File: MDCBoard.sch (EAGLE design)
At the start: 202 parts, among them J1 JUMPER-SOLDER, J10 USB-C-RECEPTACLE-KOREANHRO, J2 JUMPER-SOLDER, J3 JUMPER-SOLDER, J4 JUMPER-SOLDER, J5 BATTERY-HEADER-MOLEX-781710002, J6 JUMPER-SOLDER, J7 JUMPER-SOLDER, J8 JUMPER-SOLDER, J9 MICROSD-SOCKET, Q1 PMOS-NEXPERIA-SOT1220, Q2 PMOS-NEXPERIA-SOT1220, Q3 PMOS-NEXPERIA-SOT1220, Q4 DIODESINC-DMG2305UX, Q5 DIODESINC-DMG2305UX, Q6 DIODESINC-DMG2305UX, Q7 DIODESINC-DMG2305UX, Q8 DIODESINC-DMG2305UX, SW1 TACTILE-SWITCH, U1 TI-TPS2116, U10 TI-TPS22919DCK, U11 TI-TPS22919DCK, U12 TI-TPS22919DCK, U13 TI-TPS22919DCK, U14 TI-MSP430FR2433IRGE, U15 TI-TXB0102, U16 PANASONIC-EKMB110711X, U17 LATTICE-ICE40HX4K-BG121, U18 WINBOND-W25Q40EW, U19 NEXPERIA-74LVC1G98-OR-INV-INP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, U2 DIODESINC-AP7350, U20 NEXPERIA-74LVC1G98-BUFFER, U21 ON-AR0330CS1C12SPKA0, U22 ALLIANCE-AS4C8M16MSA-6BIN, U23 NEXPERIA-74LVC1G98-INVERTER, U24 STM-STM32F730, U25 DIODESINC-DT1446-04V-7, U3 NEXPERIA-74LVC1G98-NOR, U4 MICROCHIP-MCP7383X, U5 NEXPERIA-74LVC1G98-INVERTER, U6 EATON-STN101, U7 TI-TPS62A01, U8 TI-TPS62A01, U9 TI-TPS62A01, X1 EPSON-FC-135, X2 SITIME-SIT8021, X3 SITIME-SIT8021

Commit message: Add comment
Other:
- note added: "Pullup to VDD_USB (TPS2116's VIN1, not its VOUT as shown in the datasheet) to avoid a leakage current that would exist when battery powered. If we did pullup to VDD_A (TPS2116's VOUT), ST would be driven to GND when battery powered, and we'd have a huge leakage current between VDD_A and GND (4.2V/10k = 420uA)."
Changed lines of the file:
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@@
 measurements.
 See math to the right!</text>
+<text x="248.666" y="433.324" size="1.016" layer="95" align="top-left">Pullup to VDD_USB (TPS2116's VIN1, not its VOUT
+as shown in the datasheet) to avoid a leakage
+current that would exist when battery powered.
+If we did pullup to VDD_A (TPS2116's VOUT),
+ST would be driven to GND when battery powered,
+and we'd have a huge leakage current between
+VDD_A and GND (4.2V/10k = 420uA).</text>
 </plain>
 <instances>

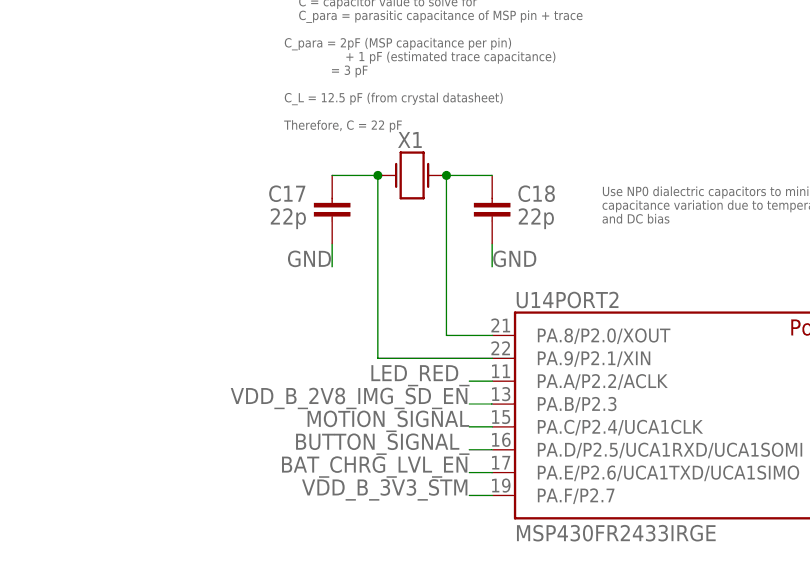
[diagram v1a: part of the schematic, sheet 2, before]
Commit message: Give names to MSP_XIN / MSP_XOUT nets
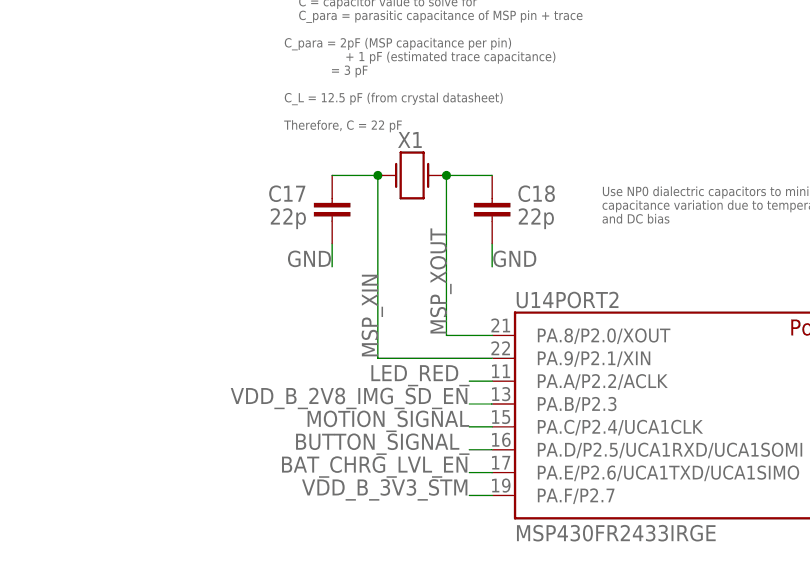
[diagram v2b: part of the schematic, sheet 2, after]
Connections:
- net N$14 renamed MSP_XIN
- net N$17 renamed MSP_XOUT
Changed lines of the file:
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@@
 </segment>
 </net>
-<net name="N$14" class="0">
+<net name="MSP_XIN" class="0">
 <segment>
 <wire x1="248.92" y1="101.6" x2="248.92" y2="81.28" width="0.1524" layer="91"/>
@@
 <junction x="248.92" y="101.6"/>
 <pinref part="U14" gate="PORT2" pin="PA.9/P2.1/XIN"/>
+<label x="248.92" y="81.28" size="1.778" layer="95" rot="R90"/>
 </segment>
 </net>
-<net name="N$17" class="0">
+<net name="MSP_XOUT" class="0">
 <segment>
 <wire x1="261.62" y1="83.82" x2="256.54" y2="83.82" width="0.1524" layer="91"/>
@@
 <junction x="256.54" y="101.6"/>
 <pinref part="U14" gate="PORT2" pin="PA.8/P2.0/XOUT"/>
+<label x="256.54" y="83.82" size="1.778" layer="95" rot="R90"/>
 </segment>
 </net>

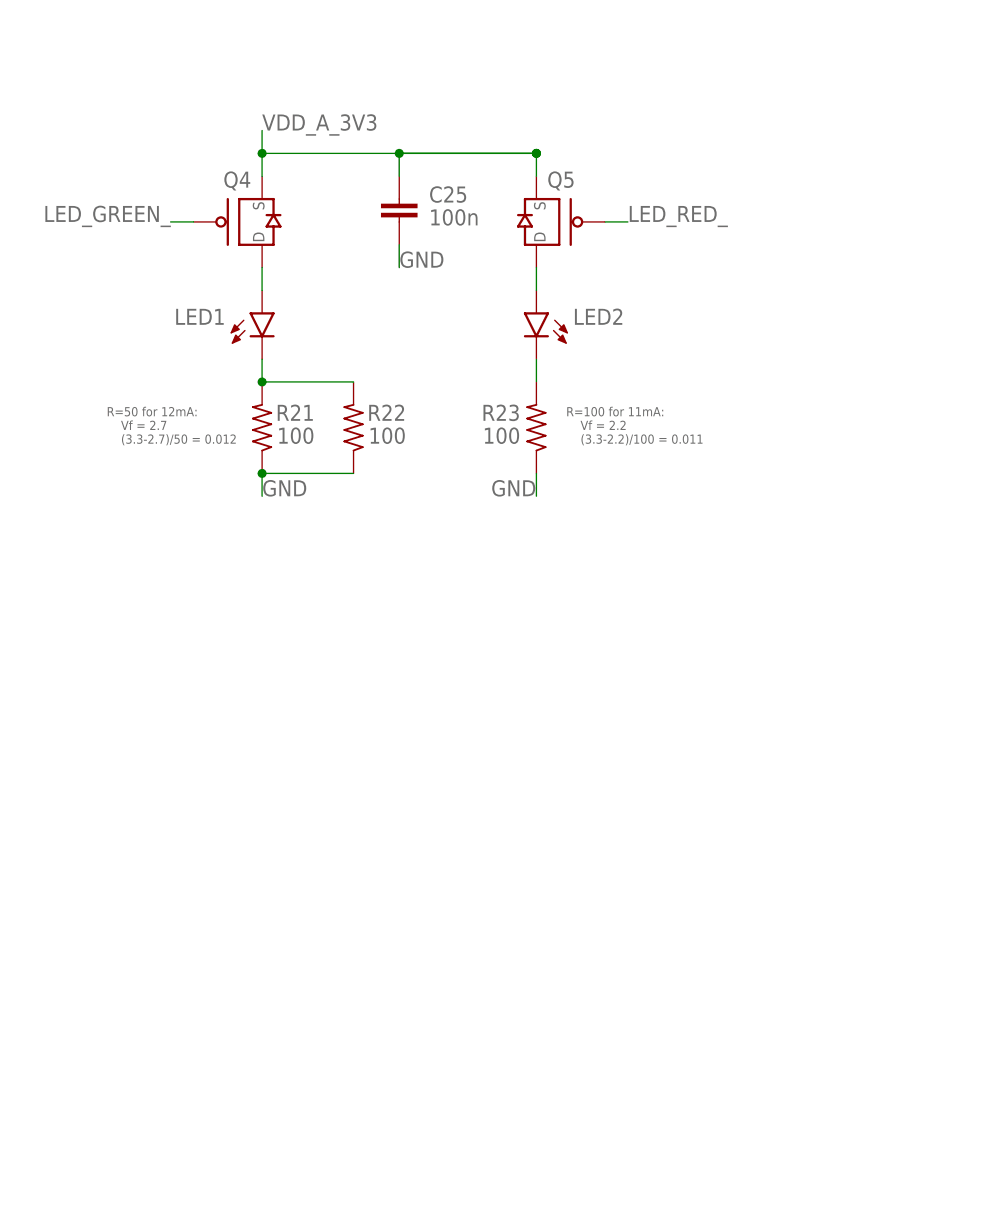
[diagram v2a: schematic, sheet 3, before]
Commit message: Replace LED drivers (Q4 and Q5) with 74LVC1G98GW,125 in the MUX configuration
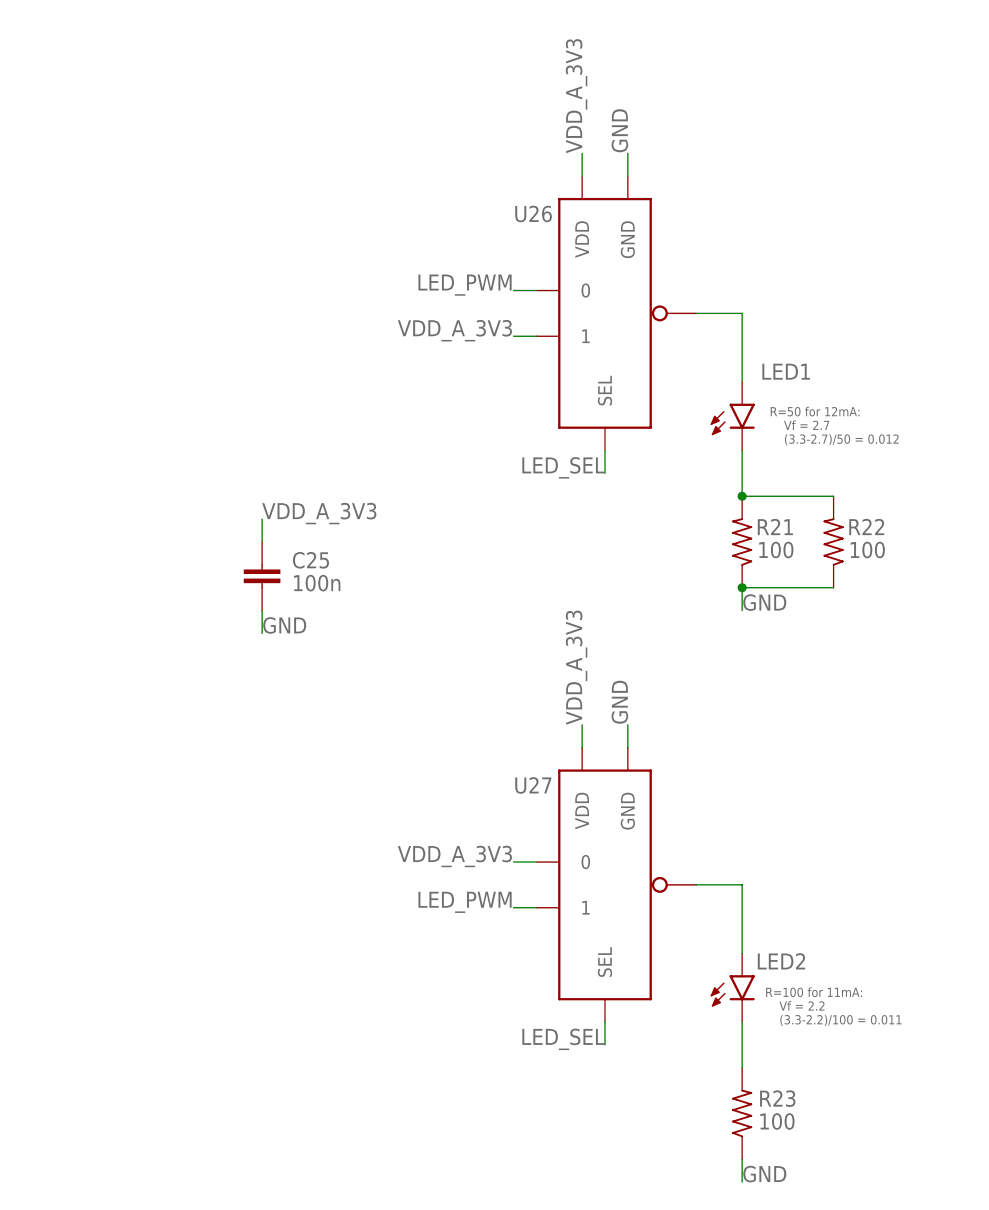
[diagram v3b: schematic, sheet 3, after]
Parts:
- removed Q4, Q5: DIODESINC-DMG2305UX, EagleLibrary:DIODESINC-DMG2305UX
- added U26, U27: NEXPERIA-74LVC1G98-MUX-INV-OUTPUT, EagleLibrary:NEXPERIA-74LVC1G98-MUX-INV-OUTPUT
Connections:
- removed net N$44: LED1.A, Q4.D
- new net LED_PWM: U26.0, U27.1
- new net LED_SEL: U26.SEL, U27.SEL
- new net N$5: LED1.A, U26.OUT
- net GND: now also U26.GND, U27.GND
- net LED_GREEN_: no longer Q4.G
- net LED_RED_: no longer Q5.G
- net N$6: now also U27.OUT; no longer Q5.D
- net VDD_A_3V3: now also U26.1, U26.VDD, U27.0, U27.VDD; no longer Q4.S, Q5.S
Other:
- moved on the sheet: C25, LED1, LED2, R21, R22, R23

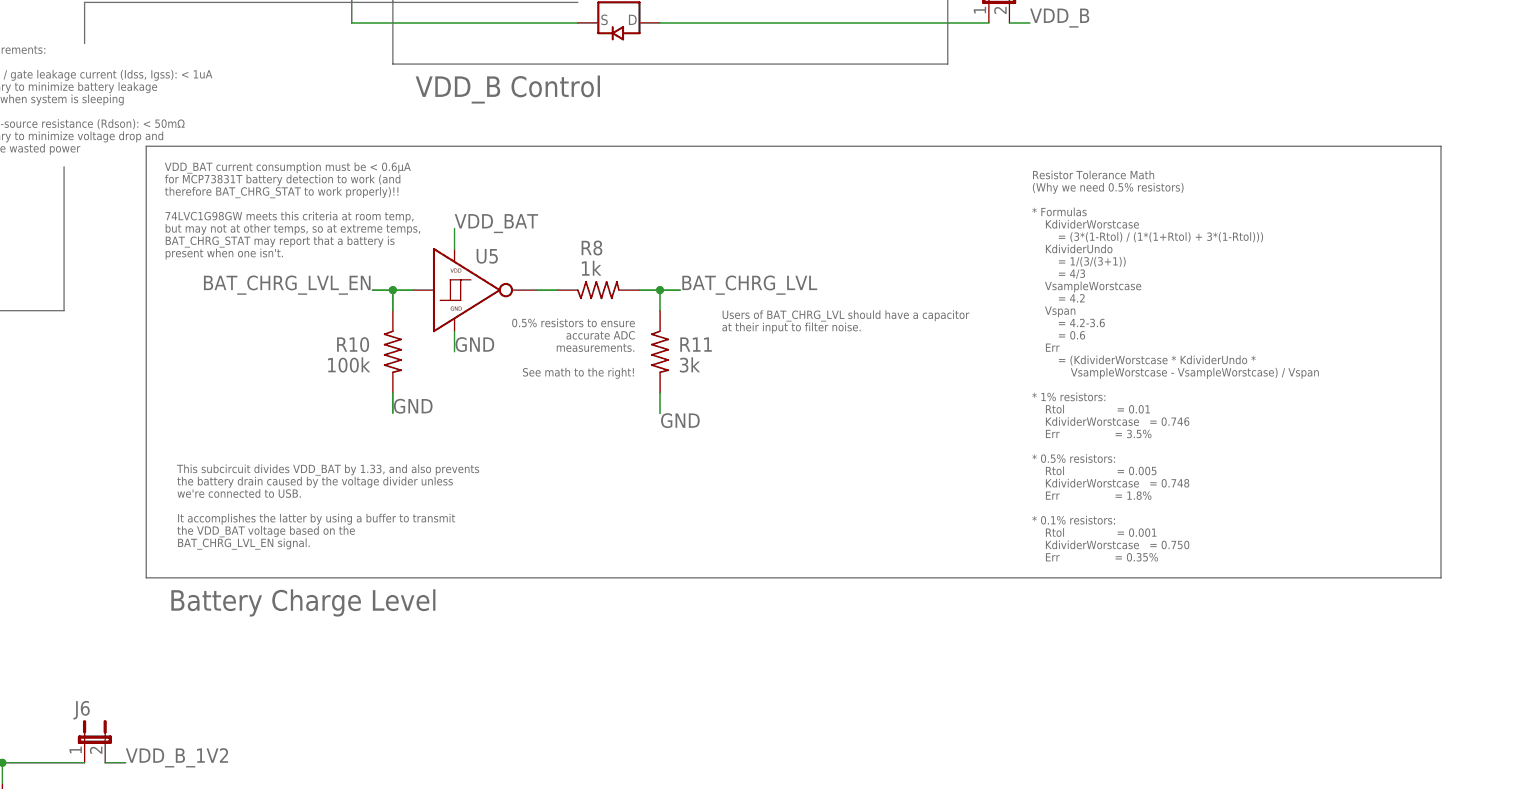
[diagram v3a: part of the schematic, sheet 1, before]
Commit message: Replace U5 with a TPS22919 load switch
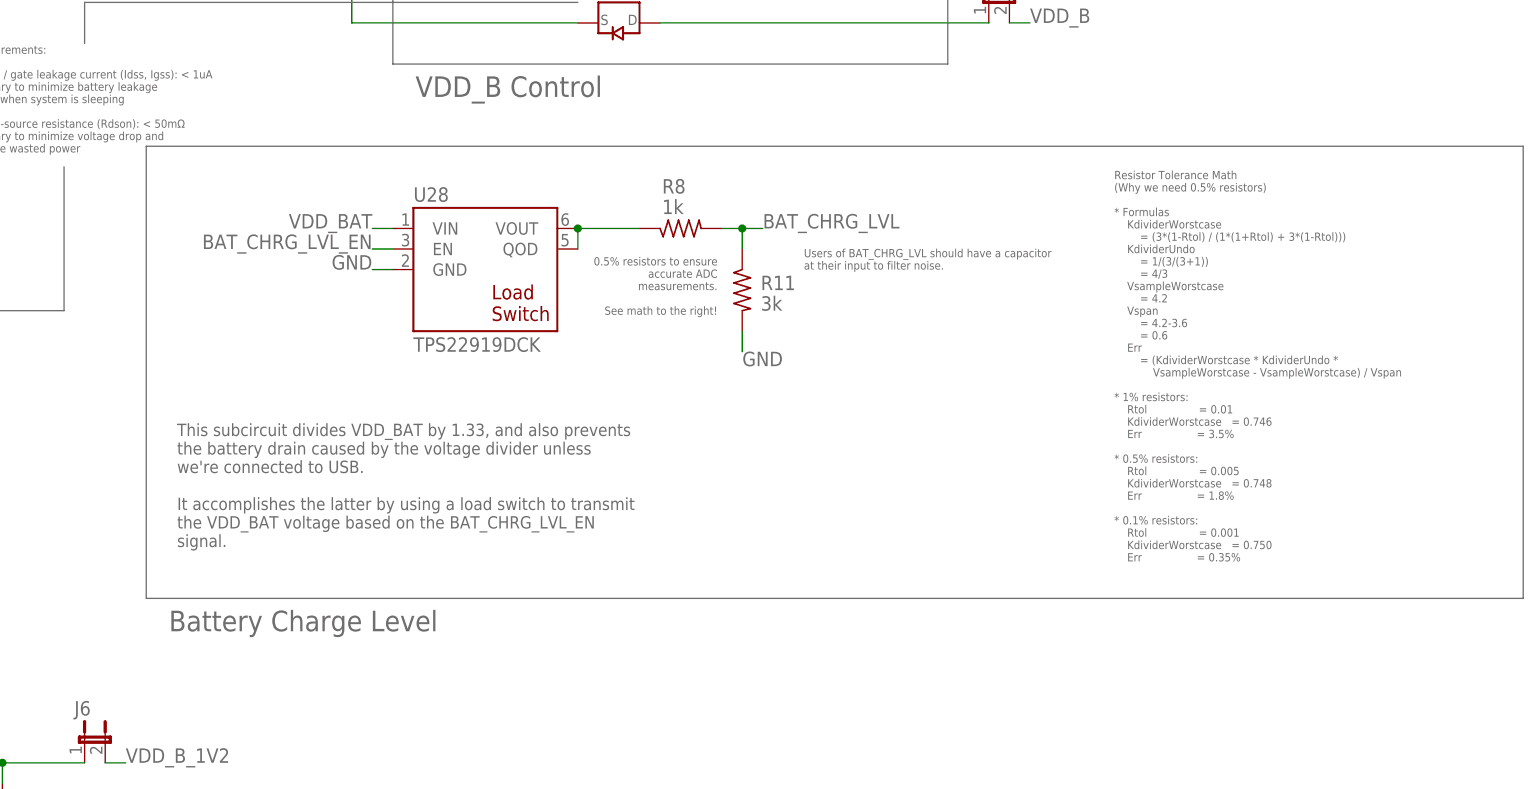
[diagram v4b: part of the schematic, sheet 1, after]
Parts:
- removed R10: 100k, EagleLibrary:RESISTOR0402
- removed U5: NEXPERIA-74LVC1G98-INVERTER, EagleLibrary:NEXPERIA-74LVC1G98-INVERTER
- added U28: TI-TPS22919DCK, EagleLibrary:TI-TPS22919DCK
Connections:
- removed net LED_GREEN_: U14PORT1.PA.1/P1.1/UCB0CLK/TA0.1/A1
- removed net LED_PWM: U26.0, U27.1
- removed net LED_RED_: U14PORT2.PA.A/P2.2/ACLK
- removed net N$9: R8.1, U5.OUT
- new net LED_SIGNAL: U14PORT1.PA.1/P1.1/UCB0CLK/TA0.1/A1, U26.0, U27.1
- new net N$17: R8.1, U28.QOD, U28.VOUT
- net BAT_CHRG_LVL_EN: now also U28.EN; no longer R10.1, U5.IN
- net GND: now also U28.GND; no longer R10.2, U5.GND
- net LED_SEL: now also U14PORT2.PA.A/P2.2/ACLK
- net VDD_BAT: now also U28.VIN; no longer U5.VDD
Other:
- note added: "This subcircuit divides VDD_BAT by 1.33, and also prevents the battery drain caused by the voltage divider unless we're connected to USB. It accomplishes the latter by using a load switch to transmit the VDD_BAT voltage based on the BAT_CHRG_LVL_EN signal."
- note removed: "This subcircuit divides VDD_BAT by 1.33, and also prevents the battery drain caused by the voltage divider unless we're connected to USB. It accomplishes the latter by using a buffer to transmit the VDD_BAT voltage based on the BAT_CHRG_LVL_EN signal."
- note removed: "VDD_BAT current consumption must be < 0.6µA for MCP73831T battery detection to work (and therefore BAT_CHRG_STAT to work properly)!! 74LVC1G98GW meets this criteria at room temp, but may not at other temps, so at extreme temps, BAT_CHRG_STAT may report that a battery is present when one isn't."
- moved on the sheet: R11, R8
